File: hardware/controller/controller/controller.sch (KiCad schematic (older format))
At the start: 9 parts, among them J1 Board Connector, J2 ICSP, J3 Power and Grinder, U1 ATmega328PB-AU

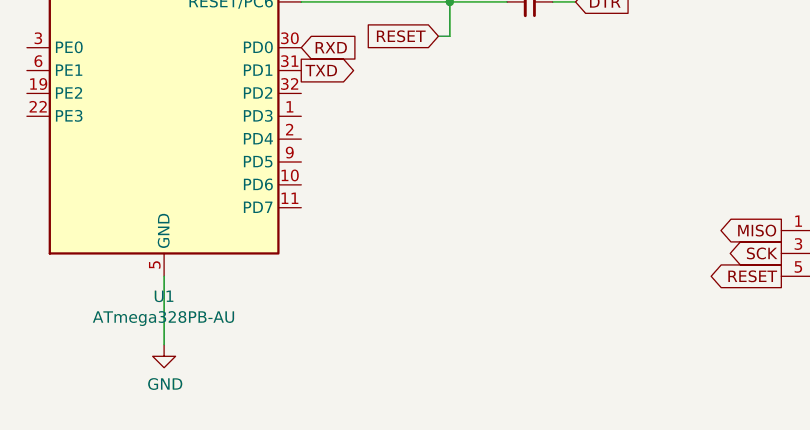
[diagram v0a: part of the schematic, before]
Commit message: Adding connector for load cell amplifier board.
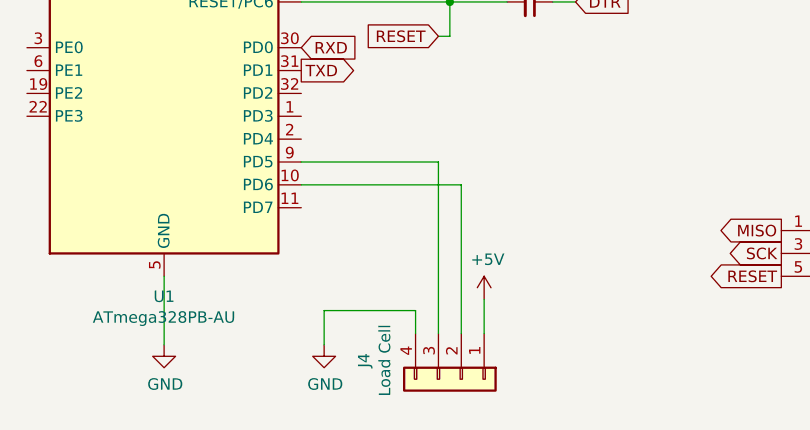
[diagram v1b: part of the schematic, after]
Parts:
- added J4: Load Cell, Connector_PinHeader_2.54mm:PinHeader_1x04_P2.54mm_Vertical, symbol Connector_Generic:Conn_01x04
- J2: footprint Connector_PinSocket_2.54mm:PinSocket_2x03_P2.54mm_Vertical -> Connector_PinHeader_2.54mm:PinHeader_2x03_P2.54mm_Vertical
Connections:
- net +5V: now also J4.1 (Pin_1)
- net GND: now also J4.4 (Pin_4)
- net at U1.10 (PD6): now also J4.2 (Pin_2)
- net at U1.9 (PD5): now also J4.3 (Pin_3)
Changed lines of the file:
@@
 F 0 "J2" H 8350 4317 50  0000 C CNN
 F 1 "ICSP" H 8350 4226 50  0000 C CNN
-F 2 "Connector_PinSocket_2.54mm:PinSocket_2x03_P2.54mm_Vertical" H 8300 4000 50  0001 C CNN
+F 2 "Connector_PinHeader_2.54mm:PinHeader_2x03_P2.54mm_Vertical" H 8300 4000 50  0001 C CNN
 F 3 "~" H 8300 4000 50  0001 C CNN
 	1    8300 4000
@@
 	1    0    0    -1
 $EndComp
+$Comp
+L Connector_Generic:Conn_01x04 J4
+U 1 1 602CAF50
+P 6700 4550
+F 0 "J4" H 6618 4125 50  0000 C CNN
+F 1 "Load Cell" H 6618 4216 50  0000 C CNN
+F 2 "Connector_PinHeader_2.54mm:PinHeader_1x04_P2.54mm_Vertical" H 6700 4550 50  0001 C CNN
+F 3 "~" H 6700 4550 50  0001 C CNN
+	1    6700 4550
+	0    1    1    0
+$EndComp
+$Comp
+L power:GND #PWR0113
+U 1 1 602CBA09
+P 6100 4400
+F 0 "#PWR0113" H 6100 4150 50  0001 C CNN
+F 1 "GND" H 6105 4227 50  0000 C CNN
+F 2 "" H 6100 4400 50  0001 C CNN
+F 3 "" H 6100 4400 50  0001 C CNN
+	1    6100 4400
+	1    0    0    -1
+$EndComp
+$Comp
+L power:+5V #PWR0114
+U 1 1 602CBFDD
+P 6800 4200
+F 0 "#PWR0114" H 6800 4050 50  0001 C CNN
+F 1 "+5V" H 6815 4373 50  0000 C CNN
+F 2 "" H 6800 4200 50  0001 C CNN
+F 3 "" H 6800 4200 50  0001 C CNN
+	1    6800 4200
+	1    0    0    -1
+$EndComp
+Wire Wire Line
+	6800 4350 6800 4200
+Wire Wire Line
+	6100 4400 6100 4250
+Wire Wire Line
+	6100 4250 6500 4250
+Wire Wire Line
+	6500 4250 6500 4350
+Wire Wire Line
+	6600 4350 6600 3600
+Wire Wire Line
+	6600 3600 6000 3600
+Wire Wire Line
+	6000 3700 6700 3700
+Wire Wire Line
+	6700 3700 6700 4350
 $EndSCHEMATC
